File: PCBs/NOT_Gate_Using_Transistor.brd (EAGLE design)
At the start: 28 x 26.8 mm, 11 parts, among them T1 BC547, T2 BC547

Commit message: Renamed files .
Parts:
- removed A, B, OUTPUT: MICROBIT_PAD, microbit:MICROBIT_PAD
- removed R3: (no value), we-rcl:R0207/7
- removed T2: BC547, transistor-neu-to92:TO92
- added IN, U$4: MICROBIT_PAD, microbit:MICROBIT_PAD
- R1: value (none) -> 10k
- R2: value (none) -> 470
- T1: device transistor-neu-to92:TO92 -> transistor:TO92
- moved T1 11.9 mm to (12.8, 12.9), turned to 0 degrees
- moved LED1 9.56 mm to (4.03, 16.9)
- moved GND 7.98 mm to (12.4, 6.90)
- moved 5V 7.87 mm to (4.33, 6.88)
- moved R2 5.28 mm to (5.52, 12.1), turned to 0 degrees
- moved R1 2.02 mm to (10.8, 17.6), turned to 0 degrees
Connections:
- removed net N$1 (its old number): R2.2, T2.2
- removed net N$2: T1.1, T2.3
- removed net N$6: A.PAD, R1.1
- removed net N$7: B.PAD, R2.1
- new net N$4: IN.PAD, R1.1
- new net VOUT: LED1.K, T1.3, U$4.PAD
- net 5V: now also R2.2; no longer T1.3
- net GND: now also T1.1; no longer LED1.K, R3.1
- net N$3: now also R2.1; no longer OUTPUT.PAD, R3.2, T2.1
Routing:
- net N$3: track 38.6 -> 5.16 mm
- net GND: track 21.9 -> 6.78 mm
- net VOUT: track 0.00 -> 14.4 mm
- net N$2: track 10.2 -> 0.00 mm
- net 5V: track 16.3 -> 7.40 mm
- net N$4: track 0.00 -> 7.48 mm
- net N$6: track 6.66 -> 0.00 mm
- net N$1 (its old number): track 5.70 -> 0.00 mm
- net N$7: track 5.21 -> 0.00 mm
- net N$1: track 7.62 -> 3.65 mm
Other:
- board size 28 x 26.8 mm -> 17.3 x 30.2 mm

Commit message: Updated
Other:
- board size 17.3 x 30.2 mm -> 23 x 30 mm
- board text added: "PinwheelRobotics"
- board text added: "care@pinwheel"
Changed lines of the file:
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@@
 <drawing>
 <settings>
-<setting alwaysvectorfont="yes"/>
+<setting alwaysvectorfont="no"/>
 <setting verticaltext="up"/>
 </settings>
-<grid distance="1" unitdist="mm" unit="mm" style="lines" multiple="1" display="yes" altdistance="0.001" altunitdist="mm" altunit="mm"/>
+<grid distance="0.5" unitdist="mm" unit="mm" style="lines" multiple="1" display="yes" altdistance="0.001" altunitdist="mm" altunit="mm"/>
 <layers>
 <layer number="1" name="Top" color="4" fill="1" visible="yes" active="yes"/>
@@
 <layer number="43" name="vRestrict" color="2" fill="10" visible="yes" active="yes"/>
 <layer number="44" name="Drills" color="7" fill="1" visible="no" active="yes"/>
-<layer number="45" name="Holes" color="7" fill="1" visible="no" active="yes"/>
+<layer number="45" name="Holes" color="7" fill="1" visible="yes" active="yes"/>
 <layer number="46" name="Milling" color="3" fill="1" visible="no" active="yes"/>
 <layer number="47" name="Measures" color="7" fill="1" visible="no" active="yes"/>
@@
 <board>
 <plain>
-<wire x1="-0.398025" y1="29.6205625" x2="-0.399934375" y2="0.793775" width="0" layer="20"/>
-<wire x1="-0.399934375" y1="0.793775" x2="0.590890625" y2="-0.19396875" width="0" layer="20" curve="90.179107"/>
-<wire x1="0.590890625" y1="-0.19396875" x2="15.3316875" y2="-0.14888125" width="0" layer="20"/>
-<wire x1="15.3316875" y1="-0.14888125" x2="16.923246875" y2="1.45181875" width="0" layer="20" curve="89.963928"/>
-<wire x1="16.923246875" y1="1.45181875" x2="16.85875" y2="28.87570625" width="0" layer="20"/>
-<wire x1="16.85875" y1="28.87570625" x2="15.687" y2="30.041815625" width="0" layer="20" curve="90.021412"/>
-<wire x1="15.687" y1="30.041815625" x2="0.000003125" y2="29.999084375" width="0" layer="20"/>
-<wire x1="0.000003125" y1="29.999084375" x2="-0.398025" y2="29.6205625" width="0" layer="20" curve="86.874065"/>
+<hole x="-1.036" y="27.912" drill="3"/>
+<hole x="18.031" y="27.961" drill="3"/>
+<hole x="-0.998" y="2.041" drill="3"/>
+<hole x="18.053" y="2.032" drill="3"/>
+<wire x1="-1.3943875" y1="0" x2="18.413571875" y2="0" width="0.1524" layer="20"/>
+<wire x1="18.413571875" y1="0" x2="20" y2="1.586428125" width="0.1524" layer="20" curve="90"/>
+<wire x1="20" y1="1.586428125" x2="20" y2="28.5579125" width="0.1524" layer="20"/>
+<wire x1="20" y1="28.5579125" x2="18.5579125" y2="30" width="0.1524" layer="20" curve="90"/>
+<wire x1="18.5579125" y1="30" x2="-1.437390625" y2="30" width="0.1524" layer="20"/>
+<wire x1="-1.437390625" y1="30" x2="-3" y2="28.437390625" width="0.1524" layer="20" curve="90"/>
+<wire x1="-3" y1="28.437390625" x2="-3" y2="1.6056125" width="0.1524" layer="20"/>
+<wire x1="-3" y1="1.6056125" x2="-1.3943875" y2="0" width="0.1524" layer="20" curve="90"/>
+<text x="-0.095" y="5.45" size="1.778" layer="21" rot="R90">PinwheelRobotics</text>
+<text x="18.588" y="24.074" size="1.778" layer="22" rot="MR270">care@pinwheel</text>
 </plain>
 <attributes>

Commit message: New Update
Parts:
- moved GND 0.62 mm to (11.8, 6.99)
- moved IN 0.50 mm to (11.8, 22.9)
- moved 5V 0.18 mm to (4.22, 7.03)
- moved U$4 0.10 mm to (4.28, 22.9)
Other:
- board size 23 x 30 mm -> 22 x 30 mm
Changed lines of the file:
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@@
 <plain>
 <hole x="-1.036" y="27.912" drill="3"/>
-<hole x="18.031" y="27.961" drill="3"/>
-<hole x="-0.998" y="2.041" drill="3"/>
-<hole x="18.053" y="2.032" drill="3"/>
-<wire x1="-1.3943875" y1="0" x2="18.413571875" y2="0" width="0.1524" layer="20"/>
-<wire x1="18.413571875" y1="0" x2="20" y2="1.586428125" width="0.1524" layer="20" curve="90"/>
-<wire x1="20" y1="1.586428125" x2="20" y2="28.5579125" width="0.1524" layer="20"/>
-<wire x1="20" y1="28.5579125" x2="18.5579125" y2="30" width="0.1524" layer="20" curve="90"/>
-<wire x1="18.5579125" y1="30" x2="-1.437390625" y2="30" width="0.1524" layer="20"/>
+<hole x="17" y="27.961" drill="3"/>
+<hole x="-1" y="2" drill="3"/>
+<hole x="17" y="2" drill="3"/>
+<wire x1="-1.3943875" y1="0" x2="17.7262875" y2="0" width="0.1524" layer="20"/>
+<wire x1="17.7262875" y1="0" x2="19" y2="1.2737125" width="0.1524" layer="20" curve="90"/>
+<wire x1="19" y1="1.2737125" x2="19" y2="29.182434375" width="0.1524" layer="20"/>
+<wire x1="19" y1="29.182434375" x2="18.182434375" y2="30" width="0.1524" layer="20" curve="90"/>
+<wire x1="18.182434375" y1="30" x2="-1.437390625" y2="30" width="0.1524" layer="20"/>
 <wire x1="-1.437390625" y1="30" x2="-3" y2="28.437390625" width="0.1524" layer="20" curve="90"/>
 <wire x1="-3" y1="28.437390625" x2="-3" y2="1.6056125" width="0.1524" layer="20"/>
@@
 </autorouter>
 <elements>
-<element name="5V" library="microbit" package="MICROBIT_PAD" value="MICROBIT_PAD" x="4.325" y="6.876" smashed="yes">
-<attribute name="NAME" x="6.512" y="9.745" size="0.6096" layer="21" font="vector"/>
-</element>
-<element name="GND" library="microbit" package="MICROBIT_PAD" value="MICROBIT_PAD" x="12.426" y="6.902" smashed="yes">
-<attribute name="NAME" x="12.2" y="10.178" size="0.4064" layer="21" font="vector"/>
-</element>
-<element name="IN" library="microbit" package="MICROBIT_PAD" value="MICROBIT_PAD" x="12.288" y="22.909" smashed="yes" rot="R180">
-<attribute name="NAME" x="11.377" y="19.469" size="0.4064" layer="21" font="vector" rot="R180"/>
+<element name="5V" library="microbit" package="MICROBIT_PAD" value="MICROBIT_PAD" x="4.222" y="7.027" smashed="yes">
+<attribute name="NAME" x="6.409" y="9.896" size="0.6096" layer="21" font="vector"/>
+</element>
+<element name="GND" library="microbit" package="MICROBIT_PAD" value="MICROBIT_PAD" x="11.809" y="6.994" smashed="yes">
+<attribute name="NAME" x="11.583" y="10.27" size="0.4064" layer="21" font="vector"/>
+</element>
+<element name="IN" library="microbit" package="MICROBIT_PAD" value="MICROBIT_PAD" x="11.792" y="22.928" smashed="yes" rot="R180">
+<attribute name="NAME" x="10.881" y="19.488" size="0.4064" layer="21" font="vector" rot="R180"/>
 </element>
 <element name="LED1" library="adafruit" library_urn="urn:adsk.eagle:library:420" package="LED3MM" package3d_urn="urn:adsk.eagle:package:6240537/1" value="" x="4.026" y="16.876" smashed="yes">
@@
 <attribute name="VALUE" x="9.694" y="13.628" size="0.6096" layer="27" font="vector" ratio="10" rot="R90"/>
 </element>
-<element name="U$4" library="microbit" package="MICROBIT_PAD" value="MICROBIT_PAD" x="4.371" y="22.906" smashed="yes" rot="R180">
-<attribute name="NAME" x="0.537" y="27.473" size="0.4064" layer="21" font="vector" rot="R270"/>
+<element name="U$4" library="microbit" package="MICROBIT_PAD" value="MICROBIT_PAD" x="4.276" y="22.925" smashed="yes" rot="R180">
+<attribute name="NAME" x="0.442" y="27.492" size="0.4064" layer="21" font="vector" rot="R270"/>
 </element>
 </elements>
@@
 <contactref element="GND" pad="PAD"/>
 <wire x1="13.8684" y1="8.2677" x2="13.8684" y2="12.8016" width="0.381" layer="1"/>
-<wire x1="12.5349" y1="6.9342" x2="13.8684" y2="8.2677" width="0.381" layer="1"/>
+<wire x1="12.92455" y1="7.32385" x2="13.8684" y2="8.2677" width="0.381" layer="1"/>
 <wire x1="13.8684" y1="12.8016" x2="14.106" y2="12.878" width="0.381" layer="1"/>
-<wire x1="12.5349" y1="6.9342" x2="12.426" y2="6.902" width="0.381" layer="1"/>
+<wire x1="12.92455" y1="7.32385" x2="11.809" y2="6.994" width="0.381" layer="1"/>
 </signal>
 <signal name="VOUT">
@@
 <wire x1="5.334" y1="16.8021" x2="5.296" y2="16.876" width="0.381" layer="1"/>
 <wire x1="5.0673" y1="22.1361" x2="5.0673" y2="17.0688" width="0.381" layer="16"/>
-<wire x1="4.5339" y1="22.6695" x2="5.0673" y2="22.1361" width="0.381" layer="16"/>
+<wire x1="4.2837125" y1="22.9196875" x2="5.0673" y2="22.1361" width="0.381" layer="16"/>
 <wire x1="5.0673" y1="17.0688" x2="5.296" y2="16.876" width="0.381" layer="16"/>
-<wire x1="4.5339" y1="22.6695" x2="4.371" y2="22.906" width="0.381" layer="16"/>
+<wire x1="4.2837125" y1="22.9196875" x2="4.276" y2="22.925" width="0.381" layer="16"/>
 </signal>
 <signal name="5V">
@@
 <contactref element="5V" pad="PAD"/>
 <wire x1="9.0678" y1="11.4681" x2="9.0678" y2="12.0015" width="0.381" layer="1"/>
-<wire x1="4.5339" y1="6.9342" x2="9.0678" y2="11.4681" width="0.381" layer="1"/>
+<wire x1="4.78299375" y1="7.18329375" x2="9.0678" y2="11.4681" width="0.381" layer="1"/>
 <wire x1="9.0678" y1="12.0015" x2="9.269" y2="12.124" width="0.381" layer="1"/>
-<wire x1="4.5339" y1="6.9342" x2="4.325" y2="6.876" width="0.381" layer="1"/>
+<wire x1="4.78299375" y1="7.18329375" x2="4.222" y2="7.027" width="0.381" layer="1"/>
 </signal>
 <signal name="N$3">
@@
 <contactref element="IN" pad="PAD"/>
 <contactref element="R1" pad="1"/>
-<wire x1="12.2682" y1="22.9362" x2="7.2009" y2="17.8689" width="0.381" layer="1"/>
+<wire x1="12.06284375" y1="22.73084375" x2="7.2009" y2="17.8689" width="0.381" layer="1"/>
 <wire x1="7.2009" y1="17.8689" x2="7.047" y2="17.636" width="0.381" layer="1"/>
-<wire x1="12.2682" y1="22.9362" x2="12.288" y2="22.909" width="0.381" layer="1"/>
+<wire x1="12.06284375" y1="22.73084375" x2="11.792" y2="22.928" width="0.381" layer="1"/>
 </signal>
 </signals>

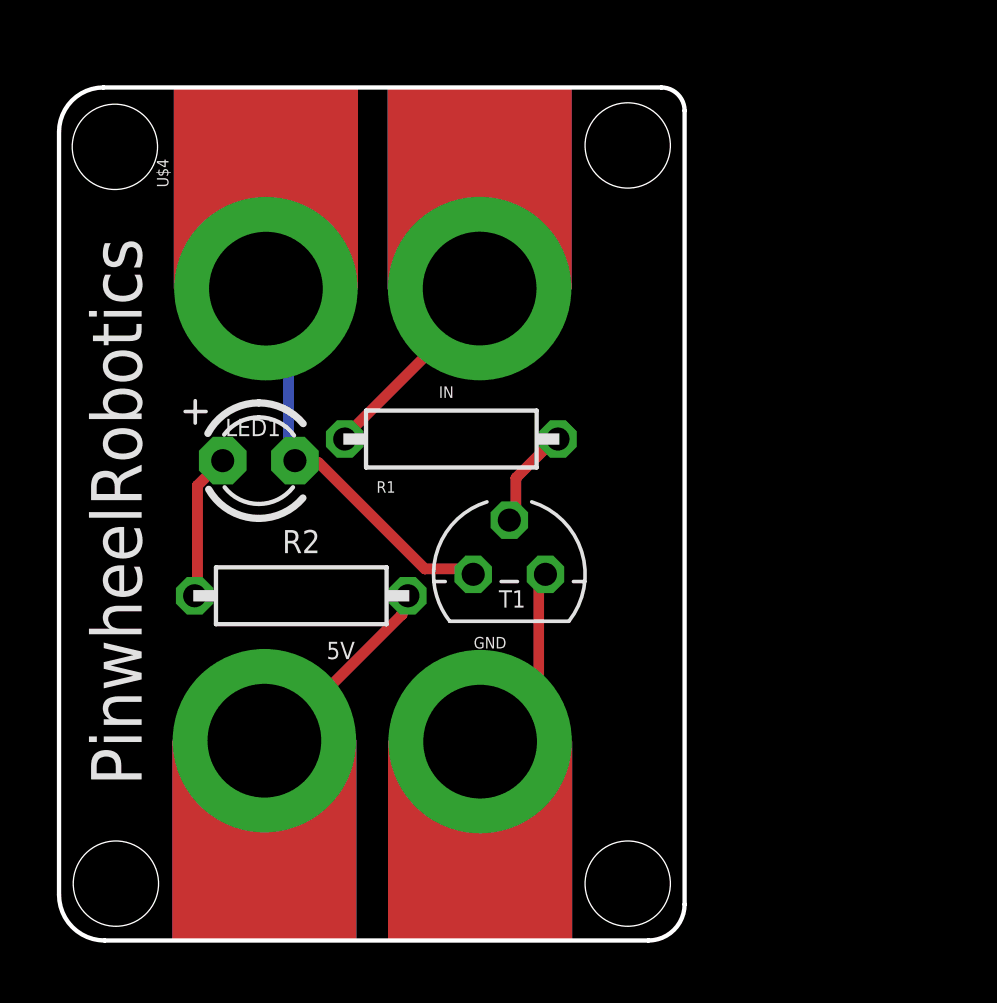
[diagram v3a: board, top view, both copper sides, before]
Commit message: Dimension added
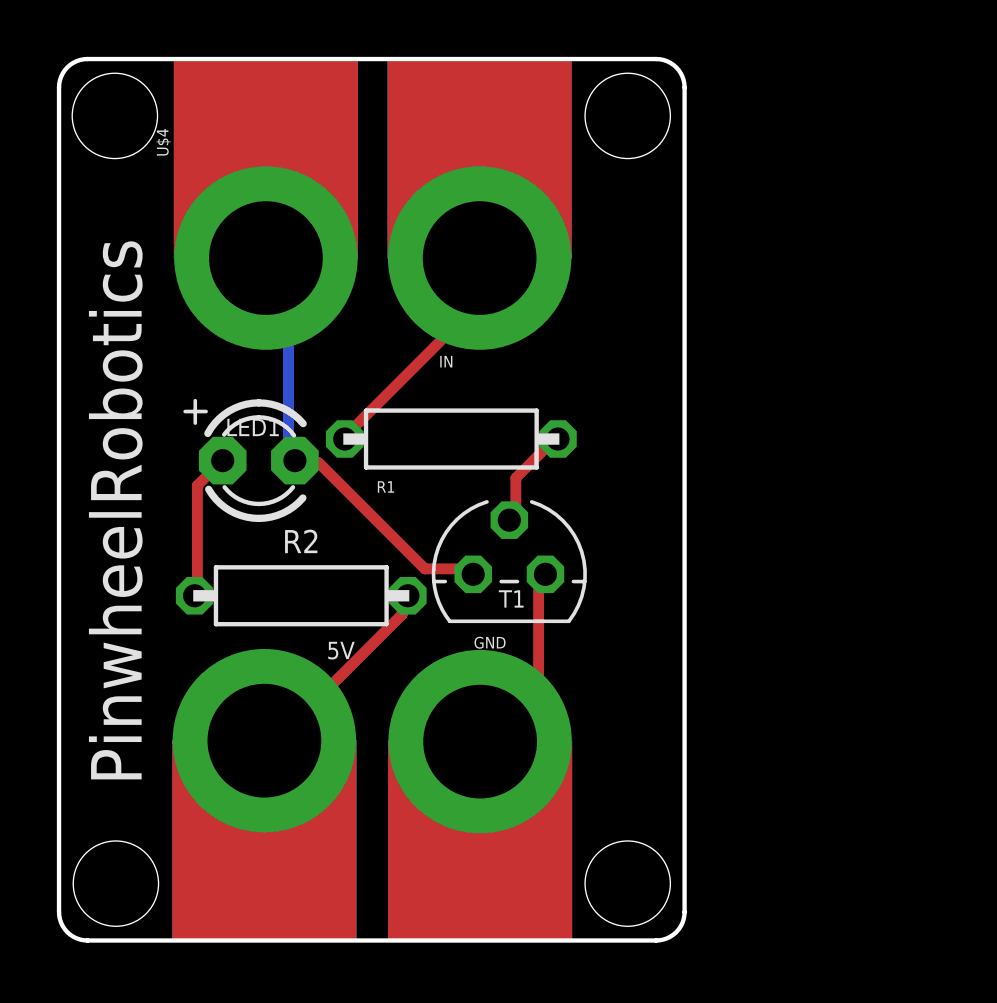
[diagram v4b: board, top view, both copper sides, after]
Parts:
- moved U$4 1.07 mm to (4.28, 24.0)
- moved IN 1.07 mm to (11.8, 24.0)
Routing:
- net VOUT: track 14.5 -> 15.5 mm
- net N$4: track 7.49 -> 8.45 mm
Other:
- board size 22 x 30 mm -> 22 x 31 mm
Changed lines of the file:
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@@
 <board>
 <plain>
-<hole x="-1.036" y="27.912" drill="3"/>
-<hole x="17" y="27.961" drill="3"/>
+<hole x="-1.036" y="29" drill="3"/>
+<hole x="17" y="29" drill="3"/>
 <hole x="-1" y="2" drill="3"/>
 <hole x="17" y="2" drill="3"/>
-<wire x1="-1.3943875" y1="0" x2="17.7262875" y2="0" width="0.1524" layer="20"/>
-<wire x1="17.7262875" y1="0" x2="19" y2="1.2737125" width="0.1524" layer="20" curve="90"/>
-<wire x1="19" y1="1.2737125" x2="19" y2="29.182434375" width="0.1524" layer="20"/>
-<wire x1="19" y1="29.182434375" x2="18.182434375" y2="30" width="0.1524" layer="20" curve="90"/>
-<wire x1="18.182434375" y1="30" x2="-1.437390625" y2="30" width="0.1524" layer="20"/>
-<wire x1="-1.437390625" y1="30" x2="-3" y2="28.437390625" width="0.1524" layer="20" curve="90"/>
-<wire x1="-3" y1="28.437390625" x2="-3" y2="1.6056125" width="0.1524" layer="20"/>
-<wire x1="-3" y1="1.6056125" x2="-1.3943875" y2="0" width="0.1524" layer="20" curve="90"/>
+<wire x1="-2" y1="0" x2="18" y2="0" width="0.1524" layer="20"/>
+<wire x1="18" y1="0" x2="19" y2="1" width="0.1524" layer="20" curve="90"/>
+<wire x1="19" y1="1" x2="19" y2="30" width="0.1524" layer="20"/>
+<wire x1="19" y1="30" x2="18" y2="31" width="0.1524" layer="20" curve="90"/>
+<wire x1="18" y1="31" x2="-2" y2="31" width="0.1524" layer="20"/>
+<wire x1="-2" y1="31" x2="-3" y2="30" width="0.1524" layer="20" curve="90"/>
+<wire x1="-3" y1="30" x2="-3" y2="1" width="0.1524" layer="20"/>
+<wire x1="-3" y1="1" x2="-2" y2="0" width="0.1524" layer="20" curve="90"/>
 <text x="-0.095" y="5.45" size="1.778" layer="21" rot="R90">PinwheelRobotics</text>
 <text x="18.588" y="24.074" size="1.778" layer="22" rot="MR270">care@pinwheel</text>
@@
 <attribute name="NAME" x="11.583" y="10.27" size="0.4064" layer="21" font="vector"/>
 </element>
-<element name="IN" library="microbit" package="MICROBIT_PAD" value="MICROBIT_PAD" x="11.792" y="22.928" smashed="yes" rot="R180">
-<attribute name="NAME" x="10.881" y="19.488" size="0.4064" layer="21" font="vector" rot="R180"/>
+<element name="IN" library="microbit" package="MICROBIT_PAD" value="MICROBIT_PAD" x="11.792" y="24" smashed="yes" rot="R180">
+<attribute name="NAME" x="10.881" y="20.56" size="0.4064" layer="21" font="vector" rot="R180"/>
 </element>
 <element name="LED1" library="adafruit" library_urn="urn:adsk.eagle:library:420" package="LED3MM" package3d_urn="urn:adsk.eagle:package:6240537/1" value="" x="4.026" y="16.876" smashed="yes">
@@
 <attribute name="VALUE" x="9.694" y="13.628" size="0.6096" layer="27" font="vector" ratio="10" rot="R90"/>
 </element>
-<element name="U$4" library="microbit" package="MICROBIT_PAD" value="MICROBIT_PAD" x="4.276" y="22.925" smashed="yes" rot="R180">
-<attribute name="NAME" x="0.442" y="27.492" size="0.4064" layer="21" font="vector" rot="R270"/>
+<element name="U$4" library="microbit" package="MICROBIT_PAD" value="MICROBIT_PAD" x="4.276" y="24" smashed="yes" rot="R180">
+<attribute name="NAME" x="0.442" y="28.567" size="0.4064" layer="21" font="vector" rot="R270"/>
 </element>
 </elements>
@@
 <wire x1="4.2837125" y1="22.9196875" x2="5.0673" y2="22.1361" width="0.381" layer="16"/>
 <wire x1="5.0673" y1="17.0688" x2="5.296" y2="16.876" width="0.381" layer="16"/>
-<wire x1="4.2837125" y1="22.9196875" x2="4.276" y2="22.925" width="0.381" layer="16"/>
+<wire x1="4.2837125" y1="22.9196875" x2="4.276" y2="24" width="0.381" layer="16"/>
 </signal>
 <signal name="5V">
@@
 <wire x1="12.06284375" y1="22.73084375" x2="7.2009" y2="17.8689" width="0.381" layer="1"/>
 <wire x1="7.2009" y1="17.8689" x2="7.047" y2="17.636" width="0.381" layer="1"/>
-<wire x1="12.06284375" y1="22.73084375" x2="11.792" y2="22.928" width="0.381" layer="1"/>
+<wire x1="12.06284375" y1="22.73084375" x2="11.792" y2="24" width="0.381" layer="1"/>
 </signal>
 </signals>
